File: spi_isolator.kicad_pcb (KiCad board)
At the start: 2 copper layers, 45.7 x 38.1 mm, 21 parts, among them K1 CONN_3, P1 CONN_2, P2 CONN_4, P3 CONN_4, T1 TRAN, U1 ADUM3471

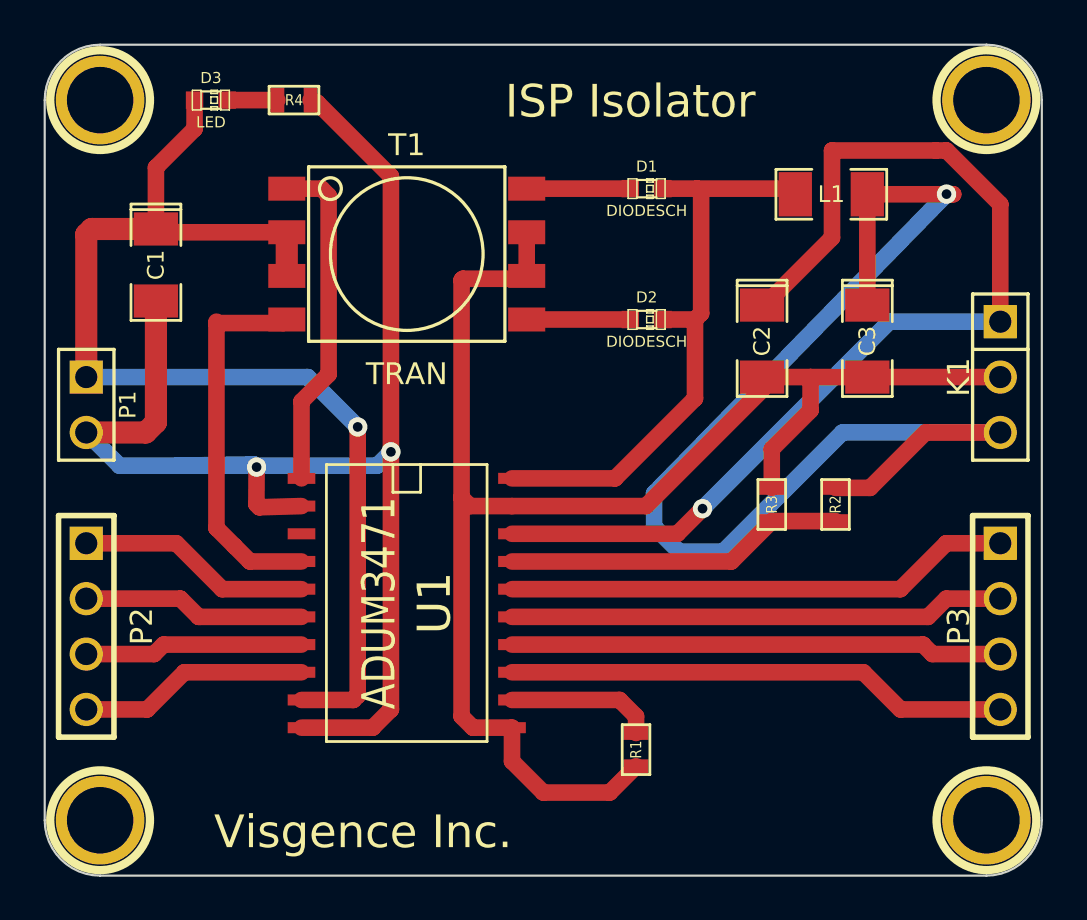
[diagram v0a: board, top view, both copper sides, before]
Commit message: Changed part on board
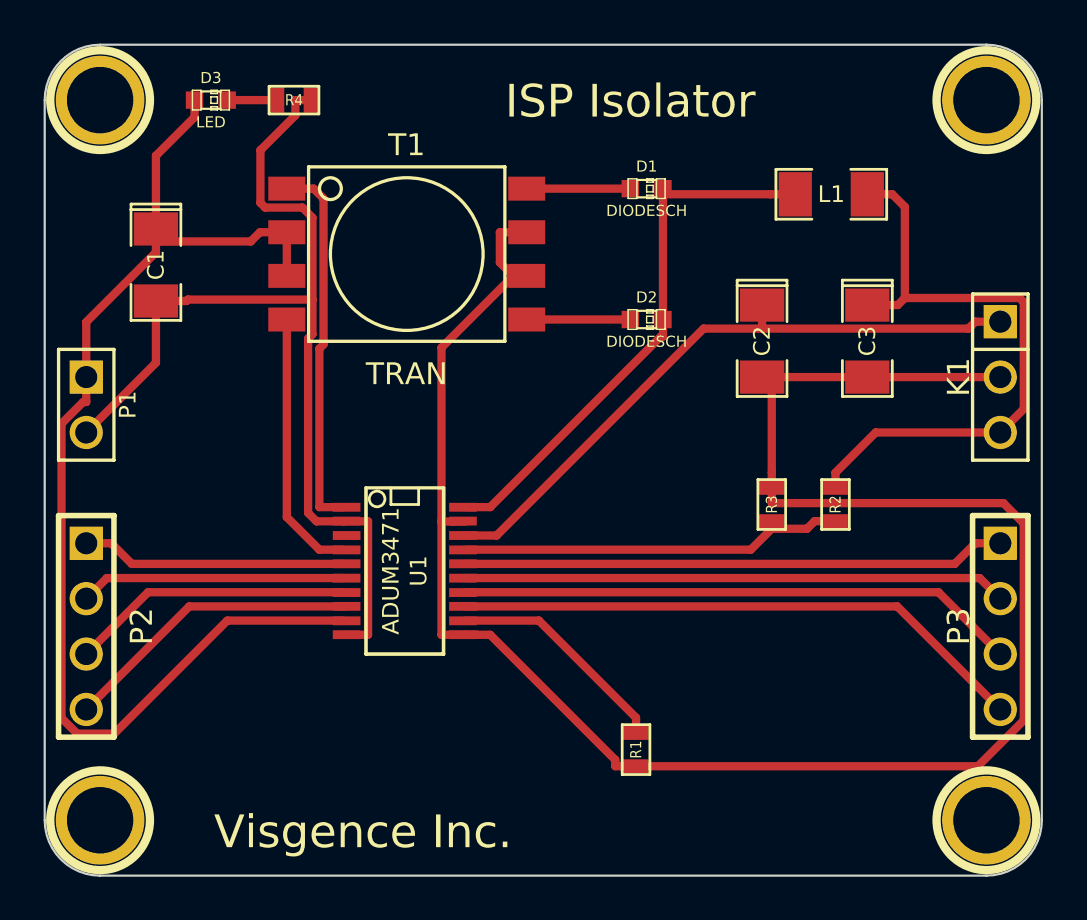
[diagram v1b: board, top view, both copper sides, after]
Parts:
- U1: footprint SO20L -> SSOP20
- h1: renamed from 1PIN; value P*** -> h1
- h2: renamed from 1PIN; value P*** -> h2
- h3: renamed from 1PIN; value P*** -> h3
- h4: renamed from 1PIN; value P*** -> h4
- moved U1 1.47 mm to (41.9, 49.5)
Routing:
- net Viso: track 57.3 -> 29.0 mm, vias 1 -> 0
- net GND: track 69.4 -> 90.9 mm
- net +5V: track 49.0 -> 29.7 mm, vias 1 -> 0
- net GNDA: track 65.4 -> 46.1 mm, vias 2 -> 0
- net N-000016: track 17.3 -> 12.3 mm
- net N-000011: track 6.76 -> 10.3 mm
- net InD: track 23.1 -> 26.5 mm
- net OutD: track 10.6 -> 13.8 mm
- net OutC: track 22.6 -> 25.7 mm
- net InC: track 10.0 -> 13.0 mm
- net N-000018: track 15.6 -> 17.8 mm
- net N-000021: track 27.4 -> 25.1 mm
- net OutB: track 22.7 -> 24.9 mm
- net InB: track 10.2 -> 12.2 mm
- net N-000015: track 15.5 -> 17.2 mm
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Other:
- net class Default: clearance 0.254 -> 0.127; trace_width 0.762 -> 0.381
- rule trace_clearance: 0.254 -> 0.127
